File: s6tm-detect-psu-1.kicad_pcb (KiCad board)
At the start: 4 copper layers, 50 x 50 mm, 120 parts, among them J1 Conn_01x02, J2 Conn_01x02, J3 USB_C_Receptacle_USB2.0_14P, J4 Conn_01x04, J5 Conn_01x04, J6 Conn_01x04_Pin, J7 TC2030, SW1 SW_Push, SW2 SW_Push, U1 TPS259470x, U2 TPS259470x, U3 TPS259470x, U4 TPS62933, U5 TPS259470x, U6 SN65HVD230, U7 HT753-1, U8 STM32F103C8Tx, Y1 8M

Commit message: pcb: finish can routing
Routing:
- net /Logic/CANH: track 6.39 -> 33.1 mm
- net /Logic/CANL: track 11.3 -> 35.4 mm
- net Net-(JP3-B): track 0.00 -> 4.69 mm
- net +3V3: track 3.10 -> 4.94 mm
- net GND: vias 101 -> 103
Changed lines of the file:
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@@
+	)
+	(via
+		(at 142.25 140.5)
+		(size 0.7)
+		(drill 0.3)
+		(layers "F.Cu" "B.Cu")
+		(free yes)
+		(net "GND")
 	)
 	(via
@@
 	)
 	(via
+		(at 142.5 129.25)
+		(size 0.7)
+		(drill 0.3)
+		(layers "F.Cu" "B.Cu")
+		(free yes)
+		(net "GND")
+	)
+	(via
 		(at 123 119.25)
 		(size 0.9)
@@
 	)
 	(segment
+		(start 130.025 144.385)
+		(end 128.385 144.385)
+		(width 0.3)
+		(layer "F.Cu")
+		(net "+3V3")
+	)
+	(segment
 		(start 126.175 106.96)
 		(end 128 106.96)
 		(width 0.2)
+		(layer "F.Cu")
+		(net "+3V3")
+	)
+	(segment
+		(start 128.385 144.385)
+		(end 128.25 144.25)
+		(width 0.3)
 		(layer "F.Cu")
 		(net "+3V3")
@@
 	)
 	(segment
+		(start 141 132)
+		(end 141 130.5)
+		(width 0.2)
+		(layer "F.Cu")
+		(net "/Logic/CANH")
+	)
+	(segment
+		(start 140.5 132.5)
+		(end 141 132)
+		(width 0.2)
+		(layer "F.Cu")
+		(net "/Logic/CANH")
+	)
+	(segment
+		(start 143.75 130.5)
+		(end 141 130.5)
+		(width 0.2)
+		(layer "F.Cu")
+		(net "/Logic/CANH")
+	)
+	(segment
 		(start 137.615 143.115)
 		(end 134.975 143.115)
@@
 	)
 	(segment
+		(start 144.75 142.75)
+		(end 144.75 131.5)
+		(width 0.2)
+		(layer "F.Cu")
+		(net "/Logic/CANH")
+	)
+	(segment
+		(start 143.5 144)
+		(end 144.75 142.75)
+		(width 0.2)
+		(layer "F.Cu")
+		(net "/Logic/CANH")
+	)
+	(segment
+		(start 135.7125 132.5)
+		(end 140.5 132.5)
+		(width 0.2)
+		(layer "F.Cu")
+		(net "/Logic/CANH")
+	)
+	(segment
 		(start 141 144)
 		(end 138.5 144)
@@
 	)
 	(segment
+		(start 144.75 131.5)
+		(end 143.75 130.5)
+		(width 0.2)
+		(layer "F.Cu")
+		(net "/Logic/CANH")
+	)
+	(segment
+		(start 141 144)
+		(end 143.5 144)
+		(width 0.2)
+		(layer "F.Cu")
+		(net "/Logic/CANH")
+	)
+	(segment
 		(start 138 142.5)
 		(end 139 141.5)
@@
 	)
 	(segment
+		(start 141 128)
+		(end 138.5 128)
+		(width 0.2)
+		(layer "F.Cu")
+		(net "/Logic/CANL")
+	)
+	(segment
+		(start 137.475 126.975)
+		(end 134.75 126.975)
+		(width 0.2)
+		(layer "F.Cu")
+		(net "/Logic/CANL")
+	)
+	(segment
+		(start 138.5 128)
+		(end 137.475 126.975)
+		(width 0.2)
+		(layer "F.Cu")
+		(net "/Logic/CANL")
+	)
+	(segment
 		(start 134.975 144.385)
 		(end 133.635 144.385)
@@
 	)
 	(segment
+		(start 142.5 141.5)
+		(end 143.5 140.5)
+		(width 0.2)
+		(layer "B.Cu")
+		(net "/Logic/CANL")
+	)
+	(segment
+		(start 143.5 140.5)
+		(end 143.5 128.75)
+		(width 0.2)
+		(layer "B.Cu")
+		(net "/Logic/CANL")
+	)
+	(segment
+		(start 143.5 128.75)
+		(end 142.75 128)
+		(width 0.2)
+		(layer "B.Cu")
+		(net "/Logic/CANL")
+	)
+	(segment
+		(start 142.75 128)
+		(end 141 128)
+		(width 0.2)
+		(layer "B.Cu")
+		(net "/Logic/CANL")
+	)
+	(segment
+		(start 141 141.5)
+		(end 142.5 141.5)
+		(width 0.2)
+		(layer "B.Cu")
+		(net "/Logic/CANL")
+	)
+	(segment
 		(start 104.75 139.25)
 		(end 103.76 138.26)
@@
 	)
 	(segment
+		(start 132.7875 132.5)
+		(end 132.7875 129.9625)
+		(width 0.2)
+		(layer "F.Cu")
+		(net "Net-(JP3-B)")
+	)
+	(segment
+		(start 133.235 129.515)
+		(end 134.75 129.515)
+		(width 0.2)
+		(layer "F.Cu")
+		(net "Net-(JP3-B)")
+	)
+	(segment
+		(start 132.7875 129.9625)
+		(end 133.235 129.515)
+		(width 0.2)
+		(layer "F.Cu")
+		(net "Net-(JP3-B)")
+	)
+	(segment

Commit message: pcb: add rgb routing
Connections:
- U8 pad 17: unconnected-(U8-PA7-Pad17) -> /Logic/RGB
- U8 pad 26: /Logic/RGB -> unconnected-(U8-PB13-Pad26)
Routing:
- net /Logic/RGB: track 0.00 -> 56.7 mm
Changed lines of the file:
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@@
 			(layers "F.Cu" "F.Mask" "F.Paste")
 			(roundrect_rratio 0.25)
-			(net "unconnected-(U8-PA7-Pad17)")
+			(net "/Logic/RGB")
 			(pinfunction "PA7_17")
-			(pintype "bidirectional+no_connect")
+			(pintype "bidirectional")
 		)
 		(pad "18" smd roundrect
@@
 			(layers "F.Cu" "F.Mask" "F.Paste")
 			(roundrect_rratio 0.25)
-			(net "/Logic/RGB")
+			(net "unconnected-(U8-PB13-Pad26)")
 			(pinfunction "PB13_26")
-			(pintype "bidirectional")
+			(pintype "bidirectional+no_connect")
 		)
 		(pad "27" smd roundrect
@@
 	)
 	(segment
+		(start 140.5 113.5)
+		(end 142.5 111.5)
+		(width 0.2)
+		(layer "F.Cu")
+		(net "/Logic/RGB")
+	)
+	(segment
+		(start 146.75 145.75)
+		(end 145.5 147)
+		(width 0.2)
+		(layer "F.Cu")
+		(net "/Logic/RGB")
+	)
+	(segment
+		(start 146.25 111.5)
+		(end 146.75 112)
+		(width 0.2)
+		(layer "F.Cu")
+		(net "/Logic/RGB")
+	)
+	(segment
+		(start 138.4125 113.5)
+		(end 140.5 113.5)
+		(width 0.2)
+		(layer "F.Cu")
+		(net "/Logic/RGB")
+	)
+	(segment
+		(start 138.5 147)
+		(end 137.465 148.035)
+		(width 0.2)
+		(layer "F.Cu")
+		(net "/Logic/RGB")
+	)
+	(segment
+		(start 146.75 112)
+		(end 146.75 145.75)
+		(width 0.2)
+		(layer "F.Cu")
+		(net "/Logic/RGB")
+	)
+	(segment
+		(start 145.5 147)
+		(end 138.5 147)
+		(width 0.2)
+		(layer "F.Cu")
+		(net "/Logic/RGB")
+	)
+	(segment
+		(start 137.465 148.035)
+		(end 137.465 151.35)
+		(width 0.2)
+		(layer "F.Cu")
+		(net "/Logic/RGB")
+	)
+	(segment
+		(start 142.5 111.5)
+		(end 146.25 111.5)
+		(width 0.2)
+		(layer "F.Cu")
+		(net "/Logic/RGB")
+	)
+	(segment

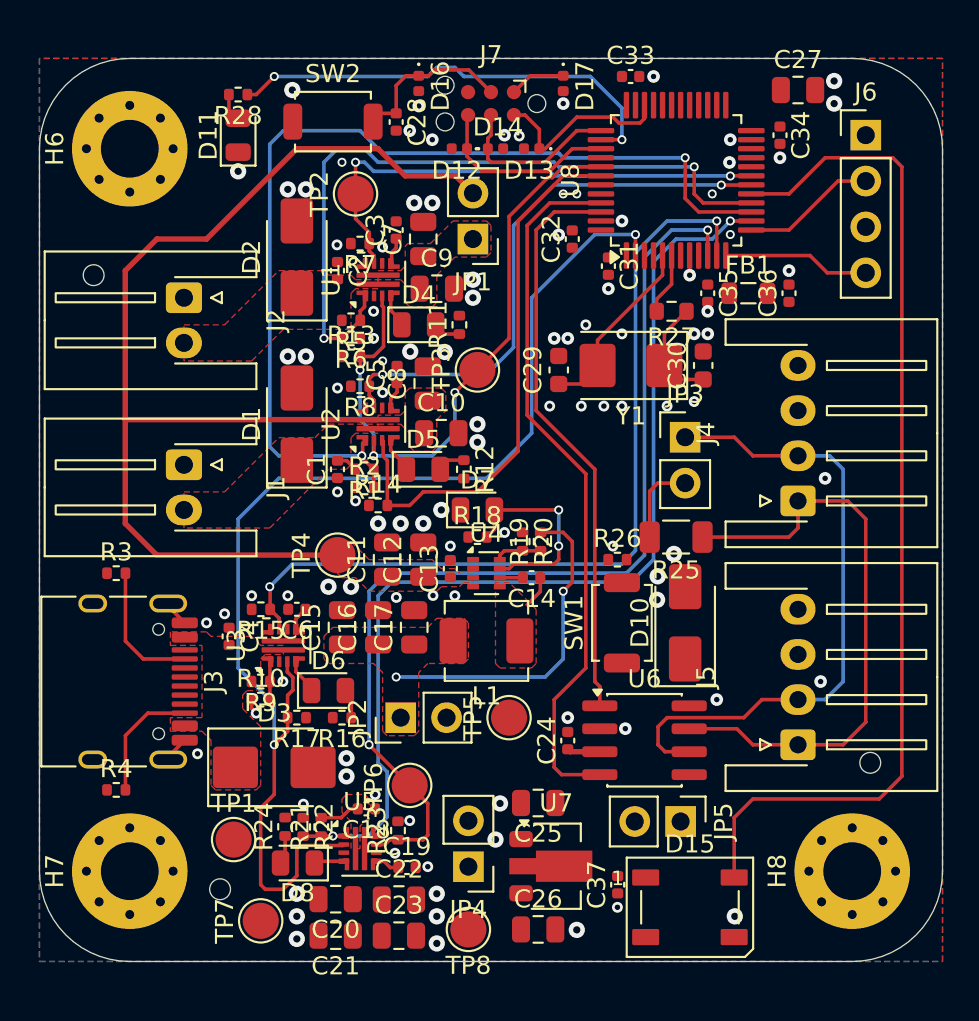
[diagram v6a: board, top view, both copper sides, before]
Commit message: pcb: add boot/rst routing
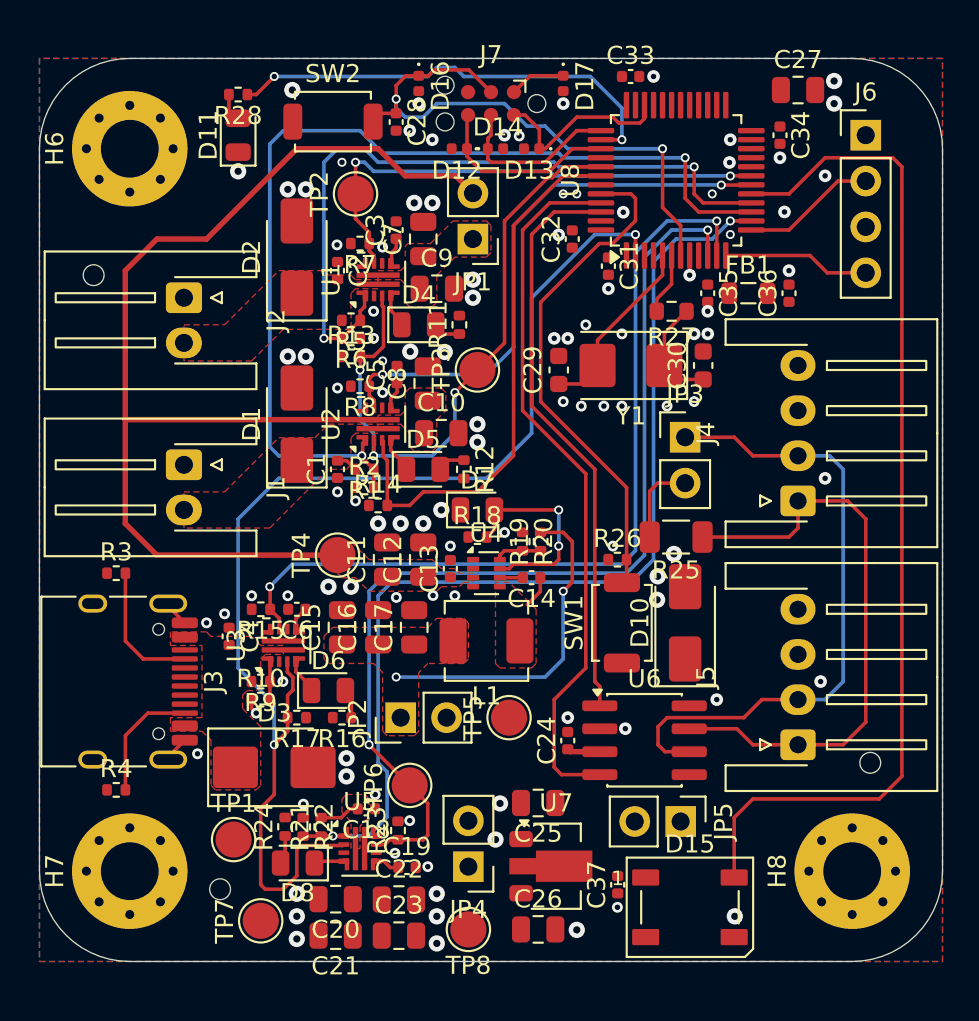
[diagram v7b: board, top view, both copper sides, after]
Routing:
- net /Logic/BOOT: track 0.00 -> 28.0 mm
- net /Logic/NRST: track 9.12 -> 32.3 mm, vias 0 -> 2
- net GND: vias 103 -> 105

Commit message: pcb: add +5v pwr routing
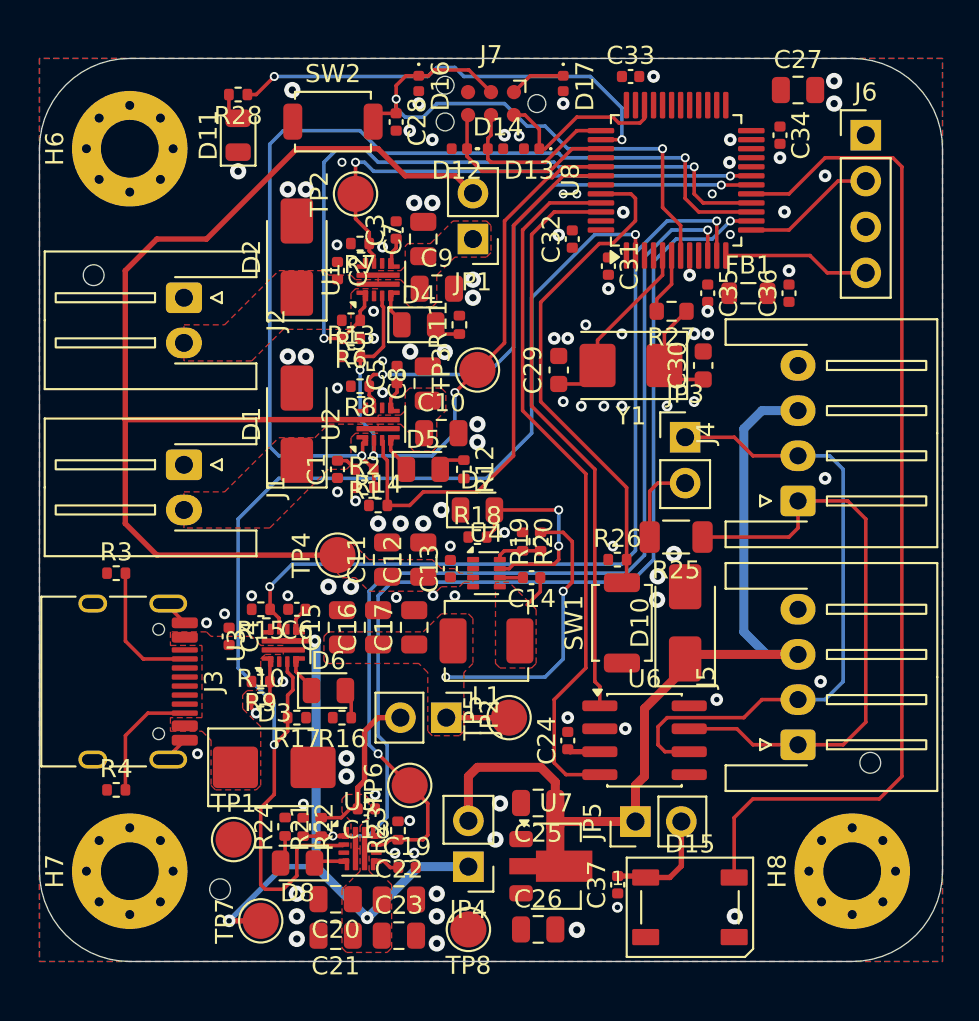
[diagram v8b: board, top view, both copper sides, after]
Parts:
- moved JP2 2.53 mm to (121.5, 142.5), turned to -90 degrees
- moved JP5 2.50 mm to (132.0, 148.2), turned to 90 degrees
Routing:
- net +5V: track 0.00 -> 92.2 mm, vias 0 -> 3
- net +5V_SMPS: track 20.6 -> 28.0 mm
- added copper zone on F.Cu, net +5V
